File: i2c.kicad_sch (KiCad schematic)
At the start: 5 parts, among them P3V317 Conn_01x02_Socket, P5V18 Conn_01x02_Socket

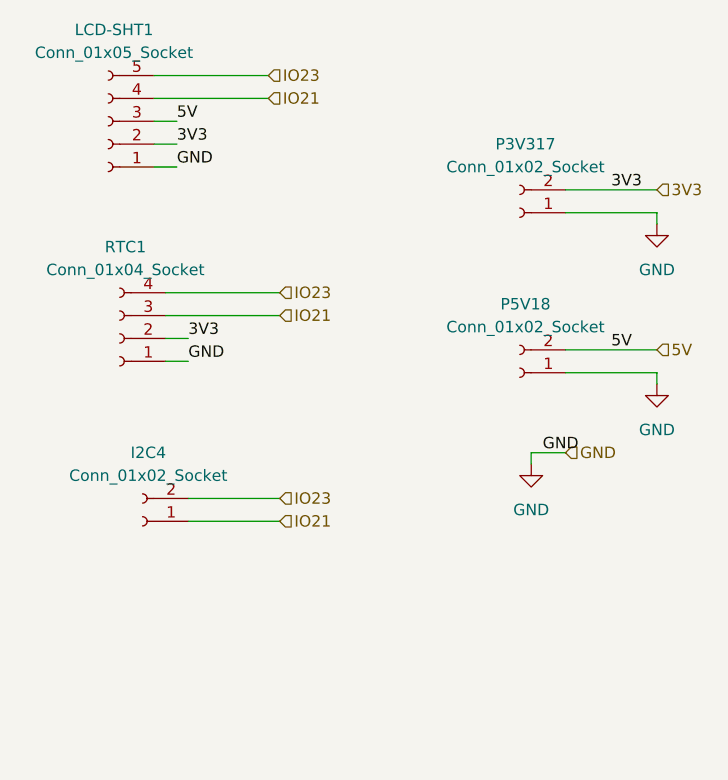
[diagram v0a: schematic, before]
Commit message: en el esquematico coloque el brakeout del shifter, genere las librerias y simbolos, modifique los sensores que trabaja a 3.3 en el esquematico
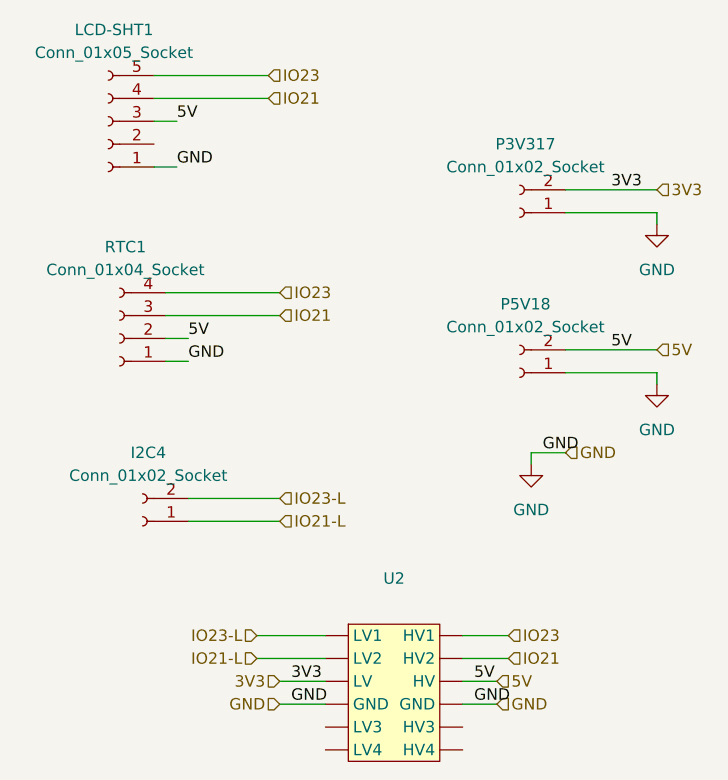
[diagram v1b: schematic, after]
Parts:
- added U2: ~, Shifter4ch:Shifter4ch, symbol Shifter:Shifter4Chanels
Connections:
- net 3V3: now also U2. (HV4); no longer LCD-SHT1.2 (Pin_2), RTC1.2 (Pin_2)
- net 5V: now also RTC1.2 (Pin_2), U2. (HV4)
- net GND: now also U2. (HV4)
- net IO21: now also U2. (HV4); no longer I2C4.1 (Pin_1)
- net IO23: now also U2. (HV4); no longer I2C4.2 (Pin_2)
- new net IO21-L: I2C4.1 (Pin_1), U2. (HV4)
- new net IO23-L: I2C4.2 (Pin_2), U2. (HV4)

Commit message: agrege los foodprints de rtc, y shifter al pcb en general, agrege un par de pistas a los i2c de 3.3, los que trabajan a 5v los deje como sda-h  y sclh
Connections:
- net 5V: now also RTC1.5 (Pin_5); no longer RTC1.2 (Pin_2)
- net IO21: now also I2C4.1 (Pin_1); no longer LCD-SHT1.4 (Pin_4), RTC1.3 (Pin_3)
- net IO23: now also I2C4.2 (Pin_2); no longer LCD-SHT1.5 (Pin_5), RTC1.4 (Pin_4)
- net IO23-H-SCL: now reaches U2. (HV4)
- net IO23-H-SCL: now also LCD-SHT1.5 (Pin_5), RTC1.4 (Pin_4)
- removed net IO21-L: I2C4.1 (Pin_1), U2. (HV4)
- removed net IO23-L: I2C4.2 (Pin_2), U2. (HV4)
- new net IO21-H-SDA: LCD-SHT1.4 (Pin_4), RTC1.3 (Pin_3), U2. (HV4)
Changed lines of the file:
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@@
 	(wire
 		(pts
-			(xy 57.15 60.96) (xy 59.69 60.96)
+			(xy 57.15 53.34) (xy 60.96 53.34)
 		)
 		(stroke
@@
 	(wire
 		(pts
-			(xy 55.88 36.83) (xy 58.42 36.83)
+			(xy 55.88 36.83) (xy 64.77 36.83)
 		)
 		(stroke
@@
 	)
 	(label "GND"
+		(at 106.68 64.77 0)
+		(effects
+			(font
+				(size 1.27 1.27)
+			)
+			(justify left bottom)
+		)
+	)
+	(label "GND"
 		(at 91.44 101.6 0)
 		(effects
@@
 	)
 	(label "5V"
-		(at 59.69 60.96 0)
+		(at 60.96 53.34 0)
 		(effects
 			(font
@@
 		)
 	)
-	(hierarchical_label "IO23-L"
+	(hierarchical_label "5V"
+		(shape input)
+		(at 64.77 36.83 0)
+		(effects
+			(font
+				(size 1.27 1.27)
+			)
+			(justify left)
+		)
+	)
+	(hierarchical_label "IO23"
 		(shape input)
 		(at 69.85 78.74 0)
@@
 		)
 	)
+	(hierarchical_label "IO23-H-SCL"
+		(shape input)
+		(at 69.85 55.88 0)
+		(effects
+			(font
+				(size 1.27 1.27)
+			)
+			(justify left)
+		)
+	)
+	(hierarchical_label "IO23-H-SCL"
+		(shape input)
+		(at 95.25 93.98 0)
+		(effects
+			(font
+				(size 1.27 1.27)
+			)
+			(justify left)
+		)
+	)
 	(hierarchical_label "IO23"
 		(shape input)
-		(at 69.85 55.88 0)
-		(effects
-			(font
-				(size 1.27 1.27)
-			)
-			(justify left)
-		)
-	)
-	(hierarchical_label "IO23"
-		(shape input)
-		(at 95.25 93.98 0)
-		(effects
-			(font
-				(size 1.27 1.27)
-			)
-			(justify left)
-		)
-	)
-	(hierarchical_label "IO23-L"
-		(shape input)
 		(at 67.31 93.98 180)
 		(effects
@@
 		)
 	)
-	(hierarchical_label "IO21-L"
+	(hierarchical_label "IO21"
 		(shape input)
 		(at 69.85 81.28 0)
@@
 		)
 	)
-	(hierarchical_label "IO21-L"
+	(hierarchical_label "IO21"
 		(shape input)
 		(at 67.31 96.52 180)
@@
 		)
 	)
-	(hierarchical_label "IO21"
+	(hierarchical_label "IO21-H-SDA"
 		(shape input)
 		(at 95.25 96.52 0)
@@
 		)
 	)
-	(hierarchical_label "IO21"
+	(hierarchical_label "IO21-H-SDA"
 		(shape input)
 		(at 69.85 58.42 0)
@@
 		)
 	)
-	(hierarchical_label "IO23"
+	(hierarchical_label "IO23-H-SCL"
 		(shape input)
 		(at 68.58 31.75 0)
@@
 		)
 	)
-	(hierarchical_label "IO21"
+	(hierarchical_label "IO21-H-SDA"
 		(shape input)
 		(at 68.58 34.29 0)
@@
 		(on_board yes)
 		(dnp no)
-		(fields_autoplaced yes)
 		(property "Reference" "U2"
 			(at 82.55 87.63 0)
@@
 		)
 		(property "Footprint" "Shifter4ch:Shifter4ch"
-			(at 95.25 92.71 0)
-			(effects
-				(font
-					(size 1.27 1.27)
-				)
-				(hide yes)
+			(at 83.82 91.186 0)
+			(effects
+				(font
+					(size 1.27 1.27)
+				)
 			)
 		)
@@
 		(on_board yes)
 		(dnp no)
-		(fields_autoplaced yes)
 		(property "Reference" "RTC1"
-			(at 52.705 50.8 0)
+			(at 52.578 48.006 0)
 			(effects
 				(font
@@
 		)
 		(property "Value" "Conn_01x04_Socket"
-			(at 52.705 53.34 0)
+			(at 52.324 50.292 0)
 			(effects
 				(font
@@
 		)
 		(property "Footprint" "Connector_PinHeader_2.54mm:PinHeader_1x04_P2.54mm_Vertical"
-			(at 52.07 60.96 0)
+			(at 48.006 69.088 0)
 			(effects
 				(font
@@
 		)
 		(property "Description" "Generic connector, single row, 01x04, script generated"
-			(at 52.07 60.96 0)
+			(at 50.038 72.39 0)
 			(effects
 				(font
@@
 		(pin "3"
 		)
+		(pin "5"
+		)
 		(instances

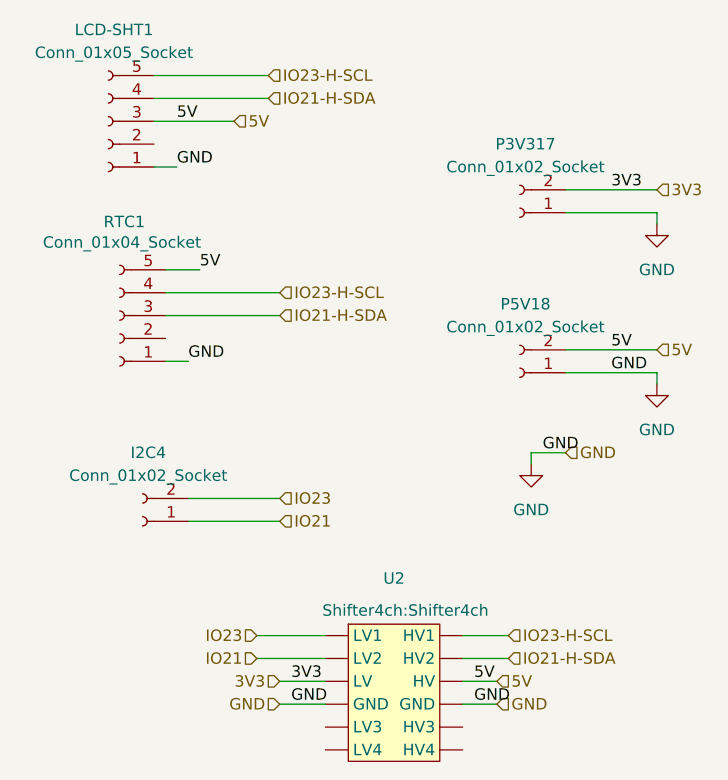
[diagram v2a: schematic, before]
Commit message: feat: integrated rtc ldc i2c / fixed 12v power line rs485 / output com pin -> input power type
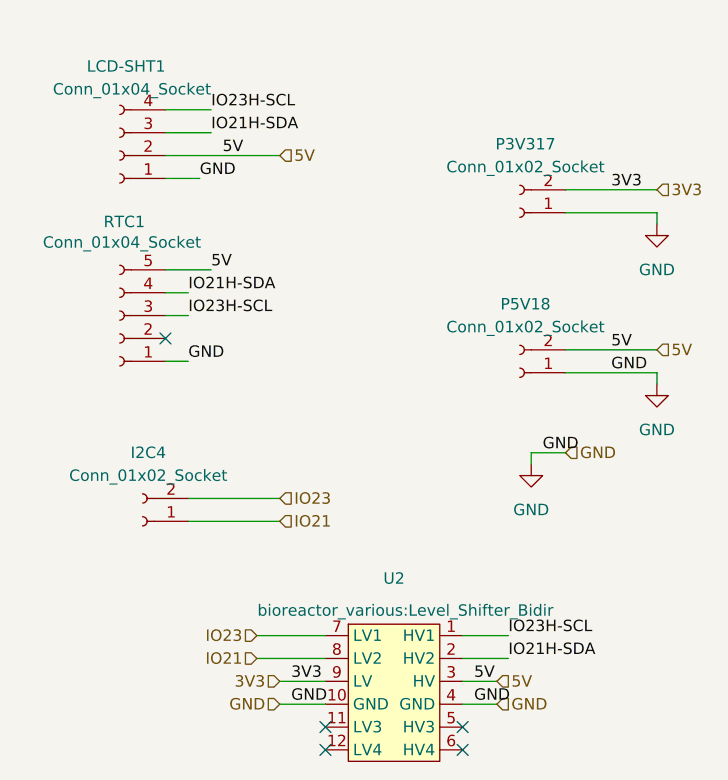
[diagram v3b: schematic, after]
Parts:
- removed LCD-SHT1: Conn_01x05_Socket, Connector_PinHeader_2.54mm:PinHeader_1x05_P2.54mm_Vertical, symbol Connector:Conn_01x05_Socket
- added LCD-SHT1: Conn_01x04_Socket, Connector_PinHeader_2.54mm:PinHeader_1x04_P2.54mm_Vertical, symbol Connector:Conn_01x04_Socket
- RTC1: footprint Connector_PinHeader_2.54mm:PinHeader_1x04_P2.54mm_Vertical -> Connector_PinHeader_2.54mm:PinHeader_1x05_P2.54mm_Vertical
- U2: footprint Shifter4ch:Shifter4ch -> bioreactor_various:Level_Shifter_Bidir
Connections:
- net 3V3: now also U2.9 (LV); no longer U2. (HV4)
- net 5V: now also U2.3 (HV), LCD-SHT1.2 (Pin_2); no longer U2. (HV4)
- net GND: now also U2.10 (GND), U2.4 (GND), LCD-SHT1.1 (Pin_1); no longer U2. (HV4)
- net IO21: now also U2.8 (LV2); no longer U2. (HV4)
- net IO23: now also U2.7 (LV1); no longer U2. (HV4)
- net IO21-H-SDA renamed IO23H-SCL
- net IO23H-SCL: now also U2.1 (HV1), LCD-SHT1.4 (Pin_4); no longer U2. (HV4)
- net IO23-H-SCL renamed IO21H-SDA
- net IO21H-SDA: now also U2.2 (HV2), LCD-SHT1.3 (Pin_3); no longer U2. (HV4)
- no-connect marks 0 -> 5

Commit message: feat: final quick fixes
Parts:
- removed P3V317, P5V18: Conn_01x02_Socket, TerminalBlock_Phoenix:TerminalBlock_Phoenix_MKDS-1,5-2_1x02_P5.00mm_Horizontal, symbol Connector:Conn_01x02_Socket

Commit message: tarjeta para raspberri, pdfs y relacion de pines
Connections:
- net 3V3: now also U2. (HV4); no longer U2.9 (LV)
- net 5V: now also U2. (HV4); no longer RTC1.5 (Pin_5), U2.3 (HV)
- net GND: now also U2. (HV4); no longer U2.10 (GND), U2.4 (GND)
- net IO21: now also U2. (HV4); no longer U2.8 (LV2)
- net IO21H-SDA: now also U2. (HV4); no longer U2.2 (HV2)
- net IO23: now also U2. (HV4); no longer U2.7 (LV1)
- net IO23H-SCL: now also U2. (HV4); no longer U2.1 (HV1)
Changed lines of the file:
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@@
 			)
 		)
-		(pin "9"
+		(pin ""
 		)
-		(pin "2"
+		(pin ""
 		)
-		(pin "8"
+		(pin ""
 		)
-		(pin "6"
+		(pin ""
 		)
-		(pin "1"
+		(pin ""
 		)
-		(pin "7"
+		(pin ""
 		)
-		(pin "11"
+		(pin ""
 		)
-		(pin "4"
+		(pin ""
 		)
-		(pin "3"
+		(pin ""
 		)
-		(pin "10"
+		(pin ""
 		)
-		(pin "12"
+		(pin ""
 		)
-		(pin "5"
+		(pin ""
 		)
 		(instances
@@
 	)
 	(symbol
-		(lib_name "Conn_01x04_Socket_1")
 		(lib_id "Connector:Conn_01x04_Socket")
 		(at 52.07 40.64 180)
@@
 		(pin "3"
 		)
-		(pin "5"
-		)
 		(instances

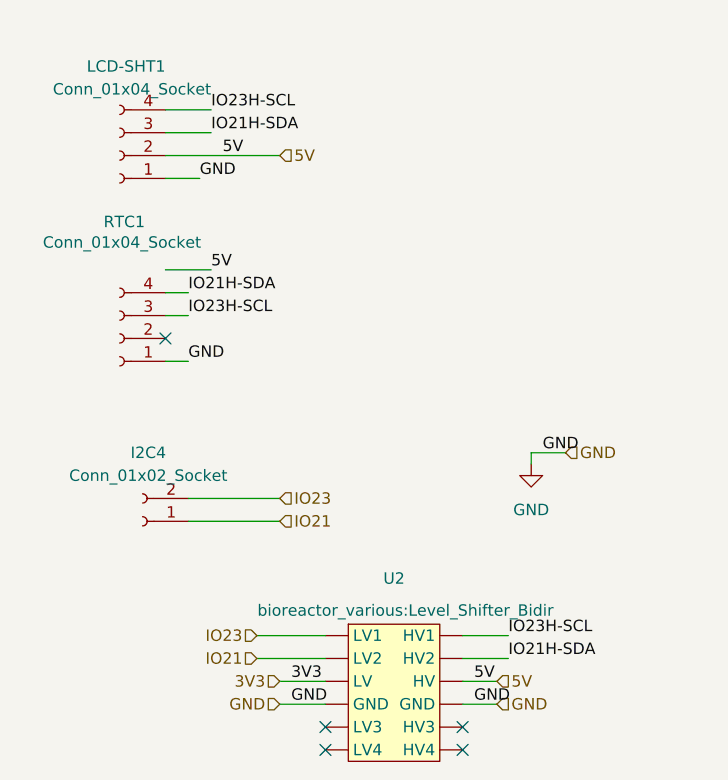
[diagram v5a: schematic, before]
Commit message: en proceso de hacer el diseño, coloque el modulo de adc a i2c por que es mas barato que comprar las piezas
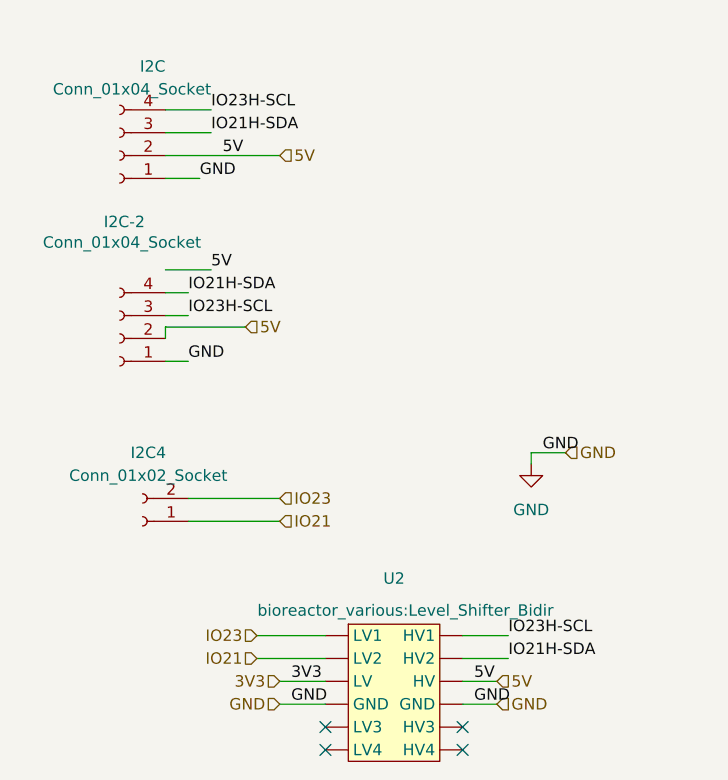
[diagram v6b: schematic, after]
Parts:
- renumbered LCD-SHT1 to I2C, RTC1 to I2C-2
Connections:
- net 5V: now also I2C-2.2 (Pin_2)
- no-connect marks 5 -> 4
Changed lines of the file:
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@@
 		(at 90.17 106.68)
 	)
-	(no_connect
-		(at 57.15 60.96)
-	)
 	(wire
 		(pts
@@
 	(wire
 		(pts
+			(xy 66.04 59.69) (xy 57.15 59.69)
+		)
+		(stroke
+			(width 0)
+			(type default)
+		)
+	)
+	(wire
+		(pts
 			(xy 90.17 93.98) (xy 95.25 93.98)
 		)
@@
 		(pts
 			(xy 67.31 93.98) (xy 74.93 93.98)
+		)
+		(stroke
+			(width 0)
+			(type default)
+		)
+	)
+	(wire
+		(pts
+			(xy 57.15 59.69) (xy 57.15 60.96)
 		)
 		(stroke
@@
 		(shape input)
 		(at 101.6 73.66 0)
+		(effects
+			(font
+				(size 1.27 1.27)
+			)
+			(justify left)
+		)
+	)
+	(hierarchical_label "5V"
+		(shape input)
+		(at 66.04 59.69 0)
 		(effects
 			(font
@@
 		(on_board yes)
 		(dnp no)
-		(property "Reference" "LCD-SHT1"
+		(property "Reference" "I2C"
 			(at 57.15 30.734 0)
 			(effects
@@
 			(project ""
 				(path "/a1c80da3-9403-4ec6-a34a-1db23a22b009/6f40c62f-5d31-4274-b02a-c88eb047bed6"
-					(reference "LCD-SHT1")
+					(reference "I2C")
 					(unit 1)
 				)
@@
 		(on_board yes)
 		(dnp no)
-		(property "Reference" "RTC1"
+		(property "Reference" "I2C-2"
 			(at 52.578 48.006 0)
 			(effects
@@
 			(project ""
 				(path "/a1c80da3-9403-4ec6-a34a-1db23a22b009/6f40c62f-5d31-4274-b02a-c88eb047bed6"
-					(reference "RTC1")
+					(reference "I2C-2")
 					(unit 1)
 				)
